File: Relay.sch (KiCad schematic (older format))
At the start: 11 parts

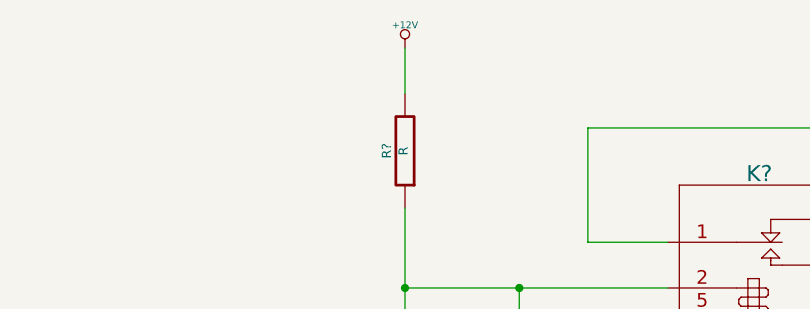
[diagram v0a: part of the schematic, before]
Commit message: 12volt net name fixed on relay schematic: use +12P instead of +12V
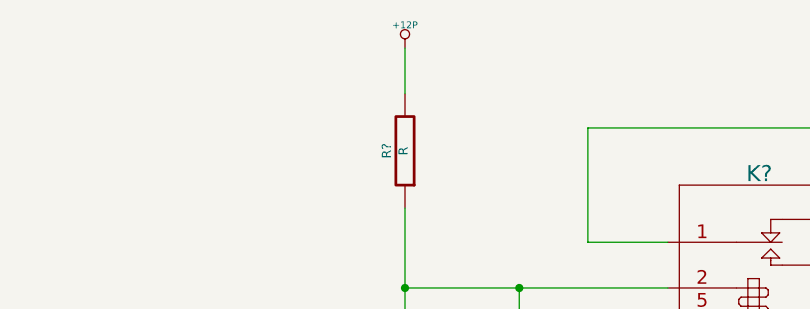
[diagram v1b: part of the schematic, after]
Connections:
- net +12V renamed +12P
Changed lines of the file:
@@
-$EndComp
-$Comp
-L +12V #PWR?
-U 1 1 52F16338
-P 5900 1500
-F 0 "#PWR?" H 5900 1450 20  0001 C CNN
-F 1 "+12V" H 5900 1600 30  0000 C CNN
-F 2 "" H 5900 1500 60  0000 C CNN
-F 3 "" H 5900 1500 60  0000 C CNN
-	1    5900 1500
-	1    0    0    -1
 $EndComp
 $Comp
@@
 Wire Wire Line
 	6100 3200 5900 3200
+$Comp
+L +12P #PWR?
+U 1 1 52F17C6A
+P 5900 1500
+F 0 "#PWR?" H 5900 1470 30  0001 C CNN
+F 1 "+12P" H 5900 1600 30  0000 C CNN
+F 2 "" H 5900 1500 60  0000 C CNN
+F 3 "" H 5900 1500 60  0000 C CNN
+	1    5900 1500
+	1    0    0    -1
+$EndComp
 $EndSCHEMATC

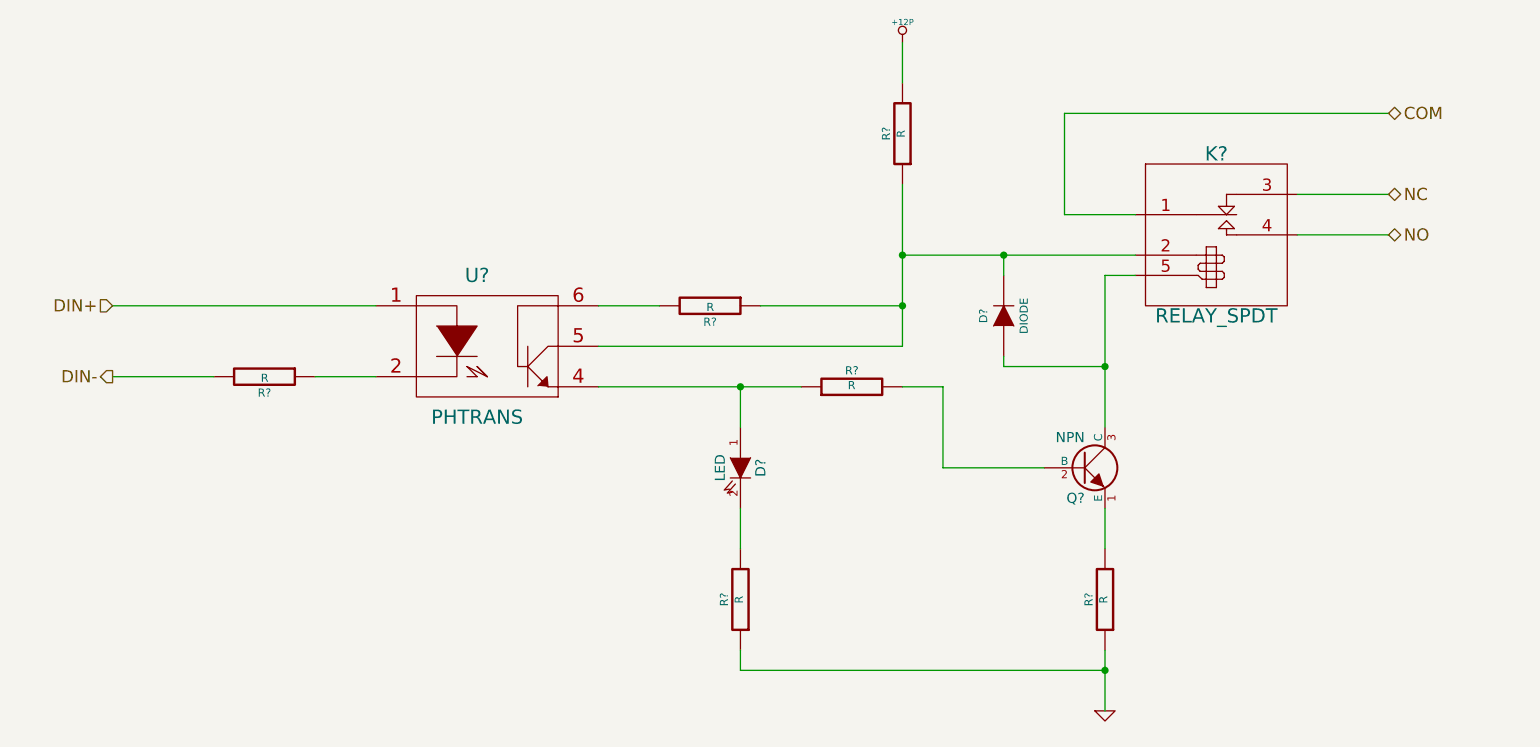
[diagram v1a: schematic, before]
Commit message: Added Arduino and top-level connections
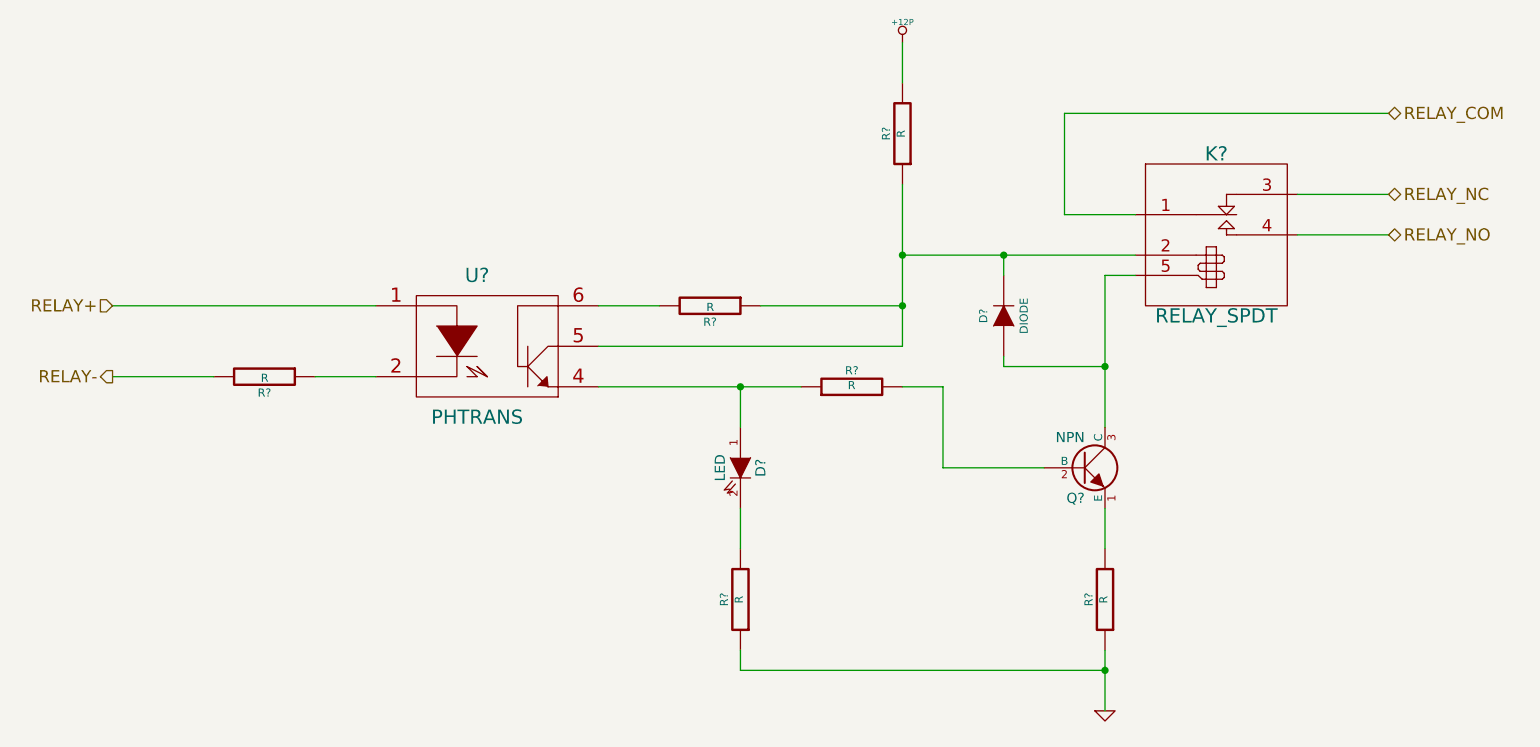
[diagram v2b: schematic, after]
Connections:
- net COM renamed RELAY_COM
- net DIN+ renamed RELAY+
- net DIN- renamed RELAY-
- net NC renamed RELAY_NC
- net NO renamed RELAY_NO
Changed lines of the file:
@@
 $EndDescr
 Text HLabel 2000 2800 0    60   Input ~ 0
-DIN+
+RELAY+
 Text HLabel 2000 3150 0    60   Output ~ 0
-DIN-
+RELAY-
 Text HLabel 8300 2250 2    60   BiDi ~ 0
-NC
+RELAY_NC
 Text HLabel 8300 2450 2    60   BiDi ~ 0
-NO
+RELAY_NO
 $Comp
 L PHTRANS U?
@@
 $EndComp
 Text HLabel 8300 1850 2    60   BiDi ~ 0
-COM
+RELAY_COM
 $Comp
 L R R?

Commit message: Added footprints for the relay module, preliminarily annotated schematic, relay components placed on PCB
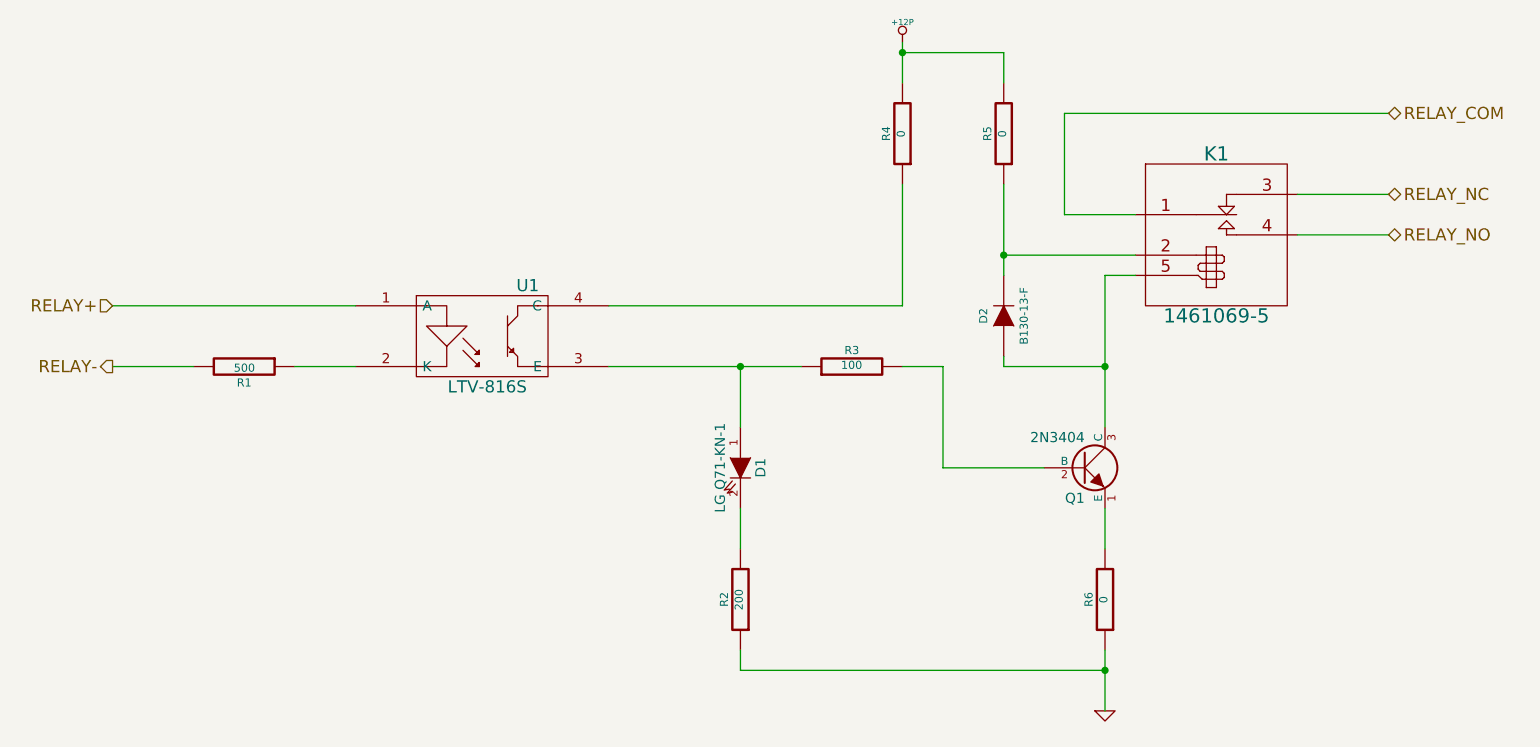
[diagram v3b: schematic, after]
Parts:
- removed R?: R, symbol R
- removed U?: PHTRANS, symbol PHTRANS
- added R5: 0, symbol R
- added U1: LTV-816S, symbol OPTO-TRANSISTOR4
- D1: renamed from D?; value LED -> LG Q71-KN-1
- D2: renamed from D?; value DIODE -> B130-13-F
- K1: renamed from K?; value RELAY_SPDT -> 1461069-5
- Q1: renamed from Q?; value NPN -> 2N3404; MFG Name (none) -> Diodes Inc; MFG Part Number (none) -> MMBT3904-7-F
- R1: renamed from R?; value R -> 500
- R2: renamed from R?; value R -> 200
- R3: renamed from R?; value R -> 100
- R4, R6: renamed from R?; value R -> 0
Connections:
- net +12P: now also R5.2
- net RELAY+: now also U1.1 (A)
- net at R1.1: now also U1.2 (K)
- net at D1.1 (A), R3.1: now also U1.3 (E)
- net at D2.2 (K), K1.2 (COIL+): now also R5.1; no longer R4.1
- new net: R4.1, U1.4 (C)
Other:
- moved on the sheet: R1, R3
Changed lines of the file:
@@
 $Descr A4 11693 8268
 encoding utf-8
-Sheet 3 9
+Sheet 2 9
 Title ""
 Date ""
@@
 Text HLabel 2000 2800 0    60   Input ~ 0
 RELAY+
-Text HLabel 2000 3150 0    60   Output ~ 0
+Text HLabel 2000 3100 0    60   Output ~ 0
 RELAY-
 Text HLabel 8300 2250 2    60   BiDi ~ 0
@@
 RELAY_NO
 $Comp
-L PHTRANS U?
-U 1 1 52F15ED8
-P 3850 3000
-F 0 "U?" H 3800 3350 70  0000 C CNN
-F 1 "PHTRANS" H 3800 2650 70  0000 C CNN
-F 2 "" H 3850 3000 60  0000 C CNN
-F 3 "" H 3850 3000 60  0000 C CNN
-	1    3850 3000
-	1    0    0    -1
-$EndComp
-$Comp
-L R R?
+L R R3
 U 1 1 52F15EEC
-P 5650 3200
-F 0 "R?" V 5730 3200 40  0000 C CNN
-F 1 "R" V 5657 3201 40  0000 C CNN
-F 2 "" V 5580 3200 30  0000 C CNN
-F 3 "" H 5650 3200 30  0000 C CNN
-	1    5650 3200
+P 5650 3100
+F 0 "R3" V 5730 3100 40  0000 C CNN
+F 1 "100" V 5657 3101 40  0000 C CNN
+F 2 "" V 5580 3100 30  0000 C CNN
+F 3 "" H 5650 3100 30  0000 C CNN
+	1    5650 3100
 	0    -1   -1   0
 $EndComp
 $Comp
-L NPN Q?
+L NPN Q1
 U 1 1 52F15F00
 P 6800 3600
-F 0 "Q?" H 6800 3450 50  0000 R CNN
-F 1 "NPN" H 6800 3750 50  0000 R CNN
+F 0 "Q1" H 6800 3450 50  0000 R CNN
+F 1 "2N3404" H 6800 3750 50  0000 R CNN
 F 2 "" H 6800 3600 60  0000 C CNN
 F 3 "" H 6800 3600 60  0000 C CNN
+F 4 "Diodes Inc" H 6800 3600 60  0001 C CNN "MFG Name"
+F 5 "MMBT3904-7-F" H 6800 3600 60  0001 C CNN "MFG Part Number"
 	1    6800 3600
 	1    0    0    -1
 $EndComp
 $Comp
-L LED D?
+L LED D1
 U 1 1 52F15F14
 P 5100 3600
-F 0 "D?" H 5100 3700 50  0000 C CNN
-F 1 "LED" H 5100 3500 50  0000 C CNN
+F 0 "D1" H 5100 3700 50  0000 C CNN
+F 1 "LG Q71-KN-1" H 5100 3500 50  0000 C CNN
 F 2 "" H 5100 3600 60  0000 C CNN
 F 3 "" H 5100 3600 60  0000 C CNN
@@
 $EndComp
 $Comp
-L RELAY_SPDT K?
+L RELAY_SPDT K1
 U 1 1 52F16219
 P 7450 2300
-F 0 "K?" H 7450 2550 70  0000 C CNN
-F 1 "RELAY_SPDT" H 7450 1750 70  0000 C CNN
+F 0 "K1" H 7450 2550 70  0000 C CNN
+F 1 "1461069-5" H 7450 1750 70  0000 C CNN
 F 2 "" H 7450 2300 60  0000 C CNN
 F 3 "" H 7450 2300 60  0000 C CNN
@@
 RELAY_COM
 $Comp
-L R R?
+L R R6
 U 1 1 52F162BB
 P 6900 4250
-F 0 "R?" V 6980 4250 40  0000 C CNN
-F 1 "R" V 6907 4251 40  0000 C CNN
+F 0 "R6" V 6980 4250 40  0000 C CNN
+F 1 "0" V 6907 4251 40  0000 C CNN
 F 2 "" V 6830 4250 30  0000 C CNN
 F 3 "" H 6900 4250 30  0000 C CNN
@@
 $EndComp
 $Comp
-L GND #PWR?
+L GND #PWR2
 U 1 1 52F162E0
 P 6900 4800
-F 0 "#PWR?" H 6900 4800 30  0001 C CNN
+F 0 "#PWR2" H 6900 4800 30  0001 C CNN
 F 1 "GND" H 6900 4730 30  0001 C CNN
 F 2 "" H 6900 4800 60  0000 C CNN
@@
 $EndComp
 $Comp
-L R R?
+L R R2
 U 1 1 52F162FC
 P 5100 4250
-F 0 "R?" V 5180 4250 40  0000 C CNN
-F 1 "R" V 5107 4251 40  0000 C CNN
+F 0 "R2" V 5180 4250 40  0000 C CNN
+F 1 "200" V 5107 4251 40  0000 C CNN
 F 2 "" V 5030 4250 30  0000 C CNN
 F 3 "" H 5100 4250 30  0000 C CNN
@@
 $EndComp
 $Comp
-L R R?
+L R R4
 U 1 1 52F16354
 P 5900 1950
-F 0 "R?" V 5980 1950 40  0000 C CNN
-F 1 "R" V 5907 1951 40  0000 C CNN
+F 0 "R4" V 5980 1950 40  0000 C CNN
+F 1 "0" V 5907 1951 40  0000 C CNN
 F 2 "" V 5830 1950 30  0000 C CNN
 F 3 "" H 5900 1950 30  0000 C CNN
@@
 	-1   0    0    1
 $EndComp
-$Comp
-L R R?
-U 1 1 52F16372
-P 4950 2800
-F 0 "R?" V 5030 2800 40  0000 C CNN
-F 1 "R" V 4957 2801 40  0000 C CNN
-F 2 "" V 4880 2800 30  0000 C CNN
-F 3 "" H 4950 2800 30  0000 C CNN
-	1    4950 2800
-	0    1    1    0
-$EndComp
 Wire Wire Line
 	7050 2350 6700 2350
@@
 	8300 2450 7850 2450
 Wire Wire Line
-	5900 2200 5900 3000
-Wire Wire Line
-	4400 3200 5400 3200
+	5900 2800 5900 2200
+Wire Wire Line
+	4450 3100 5400 3100
 Wire Wire Line
 	6900 3800 6900 4000
@@
 	6900 4500 6900 4800
 Wire Wire Line
-	5100 3200 5100 3400
-Connection ~ 5100 3200
+	5100 3100 5100 3400
+Connection ~ 5100 3100
 Wire Wire Line
 	5100 3800 5100 4000
@@
 	5900 1700 5900 1500
 Wire Wire Line
-	4400 2800 4700 2800
-Wire Wire Line
-	5900 3000 4400 3000
-Wire Wire Line
-	5200 2800 5900 2800
-Connection ~ 5900 2800
-$Comp
-L R R?
+	4450 2800 5900 2800
+$Comp
+L R R1
 U 1 1 52F163D6
-P 2750 3150
-F 0 "R?" V 2830 3150 40  0000 C CNN
-F 1 "R" V 2757 3151 40  0000 C CNN
-F 2 "" V 2680 3150 30  0000 C CNN
-F 3 "" H 2750 3150 30  0000 C CNN
-	1    2750 3150
+P 2650 3100
+F 0 "R1" V 2730 3100 40  0000 C CNN
+F 1 "500" V 2657 3101 40  0000 C CNN
+F 2 "" V 2580 3100 30  0000 C CNN
+F 3 "" H 2650 3100 30  0000 C CNN
+	1    2650 3100
 	0    1    1    0
 $EndComp
 Wire Wire Line
-	3300 3150 3000 3150
-Wire Wire Line
-	3300 2800 2000 2800
-Wire Wire Line
-	2000 3150 2500 3150
-Wire Wire Line
-	6900 3400 6900 2650
-Wire Wire Line
-	5900 2550 7050 2550
-Connection ~ 5900 2550
+	3200 3100 2900 3100
+Wire Wire Line
+	3200 2800 2000 2800
+Wire Wire Line
+	2000 3100 2400 3100
+Wire Wire Line
+	6900 2650 6900 3400
 Wire Wire Line
 	6700 2350 6700 1850
@@
 	5100 4600 6900 4600
 $Comp
-L DIODE D?
+L DIODE D2
 U 1 1 52F164E1
 P 6400 2850
-F 0 "D?" H 6400 2950 40  0000 C CNN
-F 1 "DIODE" H 6400 2750 40  0000 C CNN
+F 0 "D2" H 6400 2950 40  0000 C CNN
+F 1 "B130-13-F" H 6400 2750 40  0000 C CNN
 F 2 "" H 6400 2850 60  0000 C CNN
 F 3 "" H 6400 2850 60  0000 C CNN
@@
 $EndComp
 Wire Wire Line
-	6400 2650 6400 2550
-Connection ~ 6400 2550
+	6400 2200 6400 2650
 Wire Wire Line
 	6900 3100 6400 3100
@@
 	6600 3600 6100 3600
 Wire Wire Line
-	6100 3600 6100 3200
-Wire Wire Line
-	6100 3200 5900 3200
-$Comp
-L +12P #PWR?
+	6100 3600 6100 3100
+Wire Wire Line
+	6100 3100 5900 3100
+$Comp
+L +12P #PWR1
 U 1 1 52F17C6A
 P 5900 1500
-F 0 "#PWR?" H 5900 1470 30  0001 C CNN
+F 0 "#PWR1" H 5900 1470 30  0001 C CNN
 F 1 "+12P" H 5900 1600 30  0000 C CNN
 F 2 "" H 5900 1500 60  0000 C CNN
@@
 	1    0    0    -1
 $EndComp
+$Comp
+L OPTO-TRANSISTOR4 U1
+U 1 1 53028CD3
+P 3850 2950
+F 0 "U1" H 4050 3200 60  0000 C CNN
+F 1 "LTV-816S" H 3850 2700 60  0000 C CNN
+F 2 "" H 3850 2950 60  0000 C CNN
+F 3 "" H 3850 2950 60  0000 C CNN
+F 4 "LTV-816S" H 3850 2950 60  0001 C CNN "MFG Part Number"
+	1    3850 2950
+	1    0    0    -1
+$EndComp
+$Comp
+L R R5
+U 1 1 53028D93
+P 6400 1950
+F 0 "R5" V 6480 1950 40  0000 C CNN
+F 1 "0" V 6407 1951 40  0000 C CNN
+F 2 "" V 6330 1950 30  0000 C CNN
+F 3 "" H 6400 1950 30  0000 C CNN
+	1    6400 1950
+	-1   0    0    1
+$EndComp
+Wire Wire Line
+	6400 1700 6400 1550
+Wire Wire Line
+	6400 1550 5900 1550
+Connection ~ 5900 1550
+Wire Wire Line
+	6400 2550 7050 2550
+Connection ~ 6400 2550
 $EndSCHEMATC

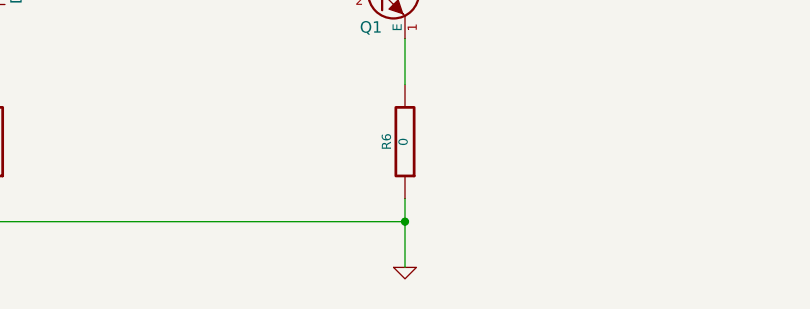
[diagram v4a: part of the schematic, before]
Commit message: Updates from Layout Work Session 4 video
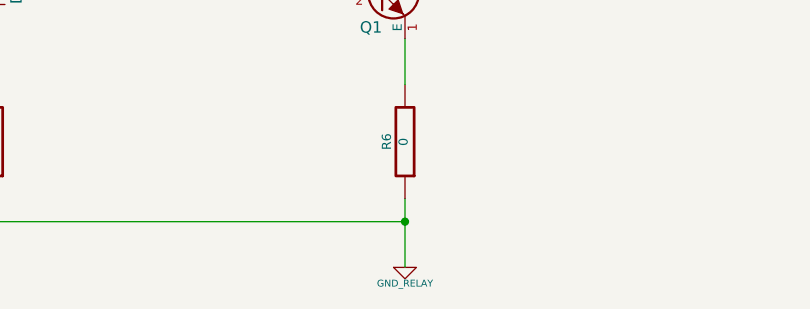
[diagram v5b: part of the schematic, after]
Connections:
- net GND renamed GND_RELAY
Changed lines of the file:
@@
-$EndComp
-$Comp
-L GND #PWR01
-U 1 1 52F162E0
-P 6900 4800
-F 0 "#PWR01" H 6900 4800 30  0001 C CNN
-F 1 "GND" H 6900 4730 30  0001 C CNN
-F 2 "" H 6900 4800 60  0000 C CNN
-F 3 "" H 6900 4800 60  0000 C CNN
-	1    6900 4800
-	1    0    0    -1
 $EndComp
 $Comp
@@
 	6100 3100 5900 3100
 $Comp
-L +12P #PWR02
+L +12P #PWR01
 U 1 1 52F17C6A
 P 5900 1500
-F 0 "#PWR02" H 5900 1470 30  0001 C CNN
+F 0 "#PWR01" H 5900 1470 30  0001 C CNN
 F 1 "+12P" H 5900 1600 30  0000 C CNN
 F 2 "" H 5900 1500 60  0000 C CNN
@@
 	6400 2550 7050 2550
 Connection ~ 6400 2550
+$Comp
+L GND_RELAY #PWR02
+U 1 1 53152624
+P 6900 4800
+F 0 "#PWR02" H 6900 4800 30  0001 C CNN
+F 1 "GND_RELAY" H 6900 4730 30  0000 C CNN
+F 2 "" H 6900 4800 60  0000 C CNN
+F 3 "" H 6900 4800 60  0000 C CNN
+	1    6900 4800
+	1    0    0    -1
+$EndComp
 $EndSCHEMATC

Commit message: Connected remaining ADC pins, some silk screen updates
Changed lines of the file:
@@
 Connection ~ 6900 4600
 Wire Wire Line
-	5900 1700 5900 1500
+	5900 1500 5900 1700
 Wire Wire Line
 	4450 2800 5900 2800
@@
 	6100 3100 5900 3100
 $Comp
-L +12P #PWR1
+L +12P #PWR01
 U 1 1 52F17C6A
 P 5900 1500
-F 0 "#PWR1" H 5900 1470 30  0001 C CNN
+F 0 "#PWR01" H 5900 1470 30  0001 C CNN
 F 1 "+12P" H 5900 1600 30  0000 C CNN
 F 2 "" H 5900 1500 60  0000 C CNN
@@
 Connection ~ 6400 2550
 $Comp
-L GND_RELAY #PWR2
+L GND_RELAY #PWR02
 U 1 1 53152624
 P 6900 4800
-F 0 "#PWR2" H 6900 4800 30  0001 C CNN
+F 0 "#PWR02" H 6900 4800 30  0001 C CNN
 F 1 "GND_RELAY" H 6900 4730 30  0000 C CNN
 F 2 "" H 6900 4800 60  0000 C CNN
